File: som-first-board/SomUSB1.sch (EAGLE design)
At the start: 22 parts, among them J1 SPARK_M.2EKEY, U1 MP2122

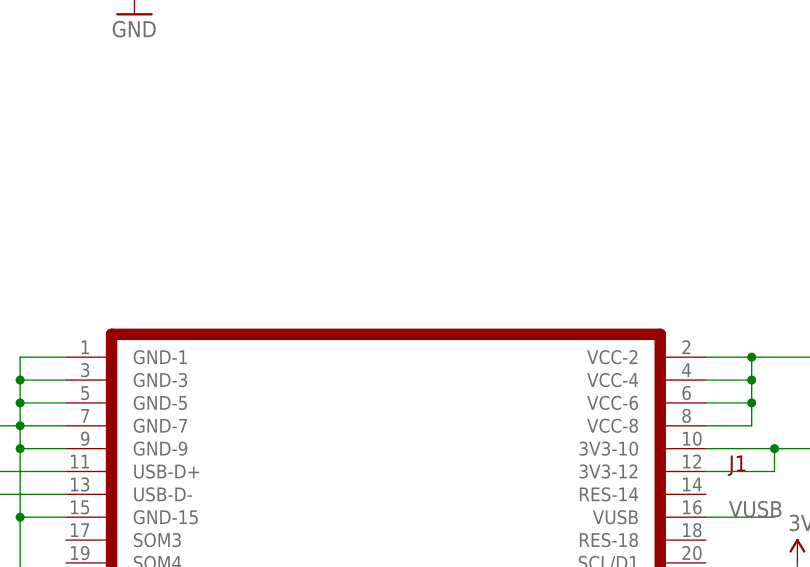
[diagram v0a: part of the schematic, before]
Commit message: Update M.2 standoff
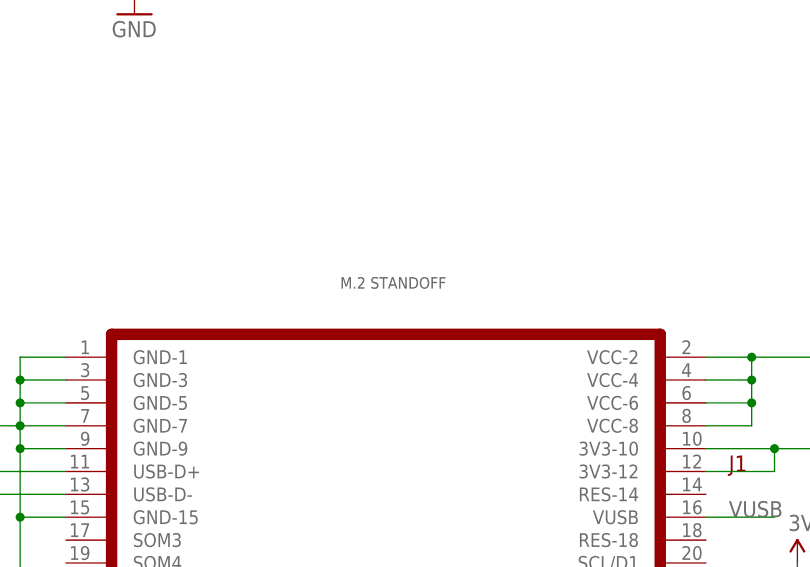
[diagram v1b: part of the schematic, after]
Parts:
- added U$1: M2-STANDOFF, rickk2:M2-STANDOFF
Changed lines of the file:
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@@
 <part name="SUPPLY5" library="rickk2" deviceset="3V7" device=""/>
 <part name="SUPPLY6" library="rickk2" deviceset="3V3" device=""/>
+<part name="U$1" library="rickk2" deviceset="M2-STANDOFF" device=""/>
 </parts>
 <sheets>
@@
 <attribute name="VALUE" x="54.864" y="196.596" size="1.778" layer="96"/>
 </instance>
+<instance part="U$1" gate="G$1" x="78.74" y="99.06" smashed="yes"/>
 </instances>
 <busses>
